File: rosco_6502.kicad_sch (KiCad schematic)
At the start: 49 parts, among them J1 UART_A, J2 UART_B, J3 Conn_01x06, J4 Conn_01x01_Male, J5 DIN41612_02x32_AC, Q1 3.6864MHz, U1 W65C02SxP, U2 MCP130-xxxHxTO, U3 SST39SF010, U4 AS6C4008-55PCN, U5 AS6C62256-55PCN, U6 XR68C681CJTR-F, U7 74HCT174, U8 ATF22V10C-7PX, U9 ATF22V10C-7PX, X1 14MHz

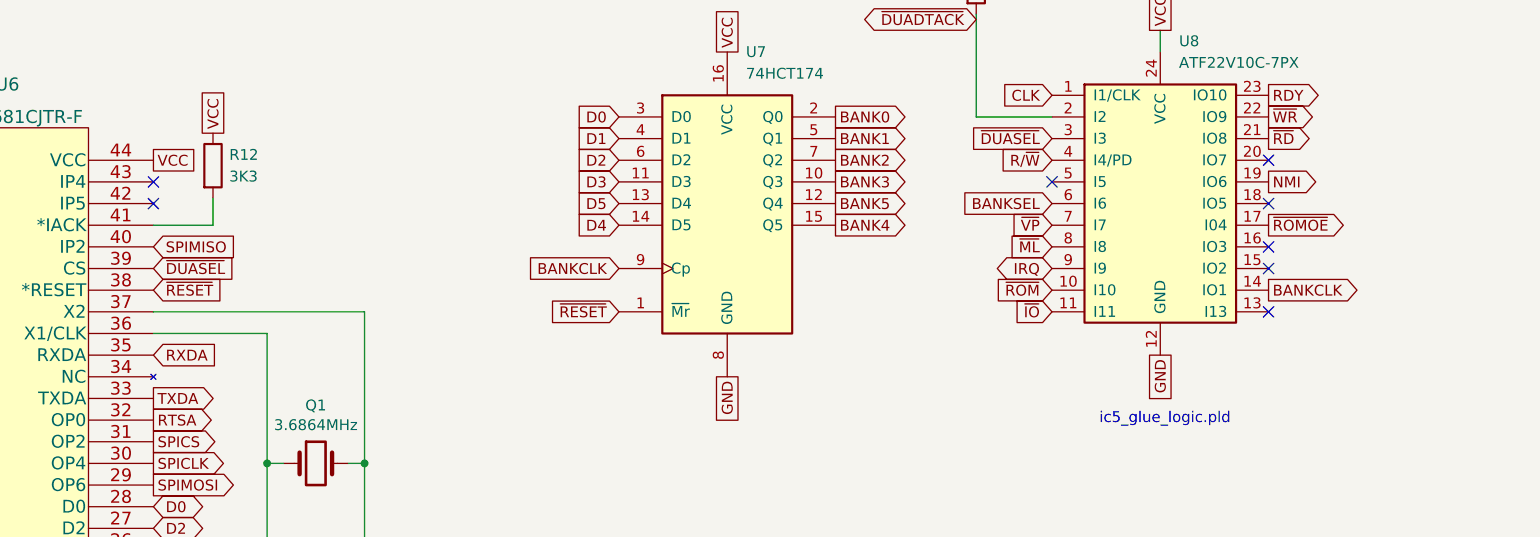
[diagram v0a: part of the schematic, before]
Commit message: Update for new DUART select logic
And some tidying up
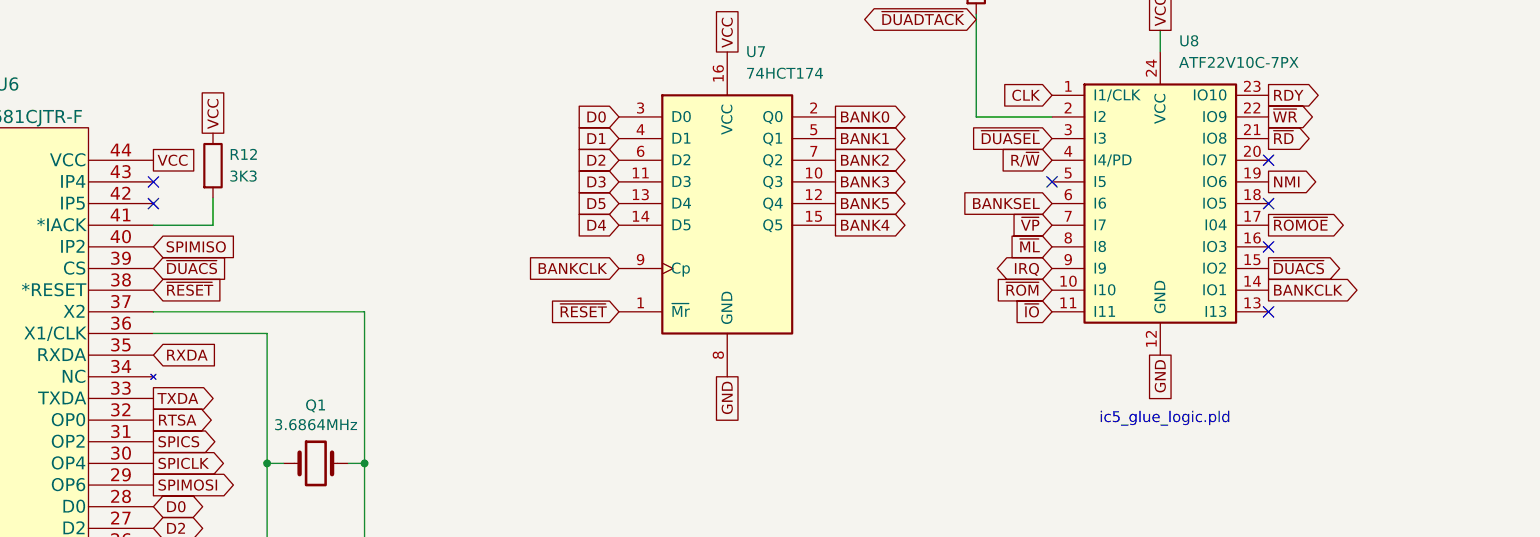
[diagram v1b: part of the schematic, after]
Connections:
- net ~{DUASEL}: no longer U6.39 (CS)
- net ~{DUACS}: now reaches U8.15 (IO2)
- net ~{DUACS}: now also U6.39 (CS)
- no-connect marks 38 -> 37
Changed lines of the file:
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@@
 	)
 	(no_connect
-		(at 228.6 152.4)
-	)
-	(no_connect
 		(at 228.6 157.48)
 	)
@@
 		)
 	)
-	(global_label "~{DUASEL}"
+	(global_label "~{DUACS}"
 		(shape input)
 		(at 97.79 152.4 0)
@@
 		)
 		(property "Intersheetrefs" "${INTERSHEET_REFS}"
-			(at 107.2788 152.3206 0)
+			(at 106.9438 152.4 0)
 			(effects
 				(font
@@
 				(hide yes)
 			)
+		)
+	)
+	(global_label "~{DUACS}"
+		(shape output)
+		(at 228.6 152.4 0)
+		(fields_autoplaced yes)
+		(effects
+			(font
+				(size 1.27 1.27)
+			)
+			(justify left)
+		)
+		(property "Intersheetrefs" "${INTERSHEET_REFS}"
+			(at 237.7538 152.4 0)
+			(effects
+				(font
+					(size 1.27 1.27)
+				)
+				(justify left)
+				(hide yes)
+			)

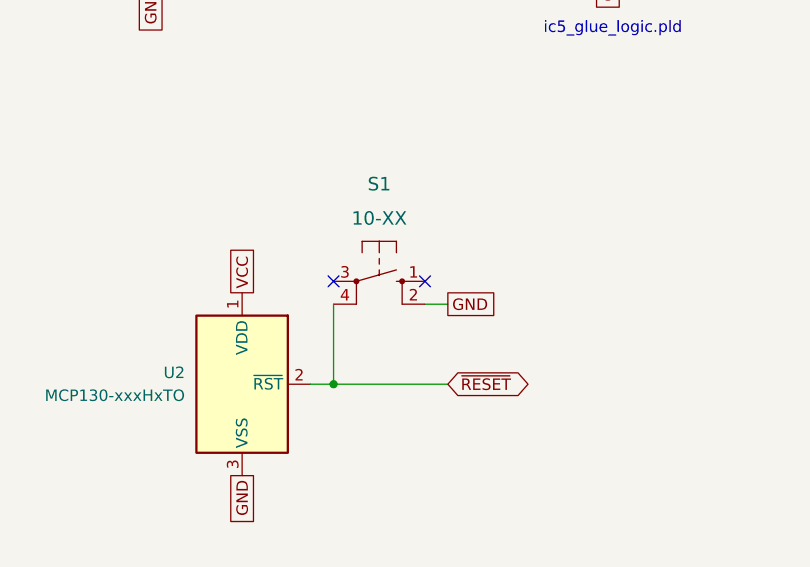
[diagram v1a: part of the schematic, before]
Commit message: SMD components replaced with THT
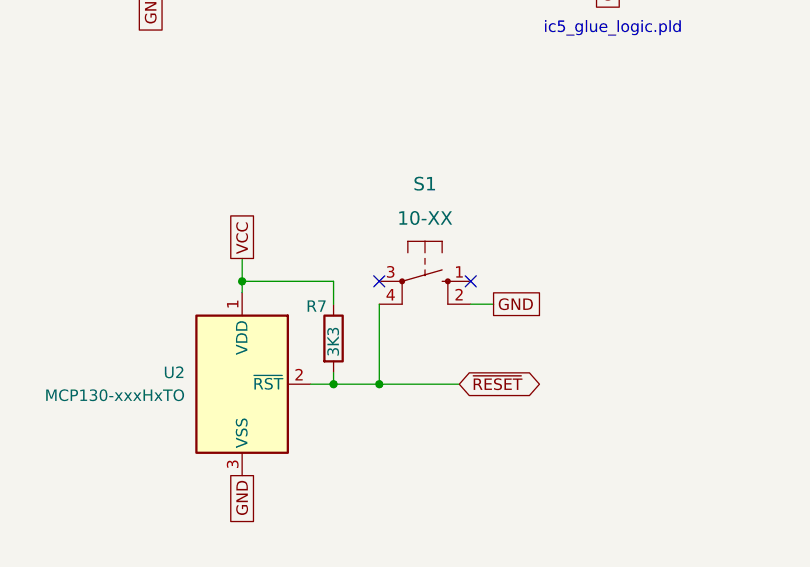
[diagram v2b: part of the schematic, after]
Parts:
- added R7: 3K3, Resistor_THT:R_Axial_DIN0204_L3.6mm_D1.6mm_P7.62mm_Horizontal, symbol Device:R
- C1, C10, C11, C12, C13, C14, C15, C2, C3, C4, C8, C9: footprint Capacitor_SMD:C_0603_1608Metric_Pad1.08x0.95mm_HandSolder -> Capacitor_THT:C_Disc_D3.0mm_W1.6mm_P2.50mm
- JP4, JP5, JP6: footprint Jumper:SolderJumper-3_P1.3mm_Bridged2Bar12_RoundedPad1.0x1.5mm -> Jumper:SolderJumper-3_P1.3mm_Open_RoundedPad1.0x1.5mm_NumberLabels; now left out of the parts list
- R1, R11, R12, R13, R2, R3, R4, R5, R6: footprint Resistor_SMD:R_0603_1608Metric_Pad0.98x0.95mm_HandSolder -> Resistor_THT:R_Axial_DIN0204_L3.6mm_D1.6mm_P7.62mm_Horizontal
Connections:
- net VCC: now also R7.1
- net ~{RESET}: now also R7.2
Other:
- moved on the sheet: S1
